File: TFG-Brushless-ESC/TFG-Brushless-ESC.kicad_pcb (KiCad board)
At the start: 2 copper layers, 66 parts, among them J2 USB C Receptacle, J3 SWD, Q1 IRF1310, Q2 IRF1310, Q3 IRF1310, Q4 IRF1310, Q5 IRF1310, Q6 IRF1310, SW1 BOOT0, SW2 NRST, SW3 USER, U1 LM317, U2 STM32F411CEUx, U3 IR2101, U4 IR2101, U5 IR2101, Y1 25MHz, Y2 32.768kHz

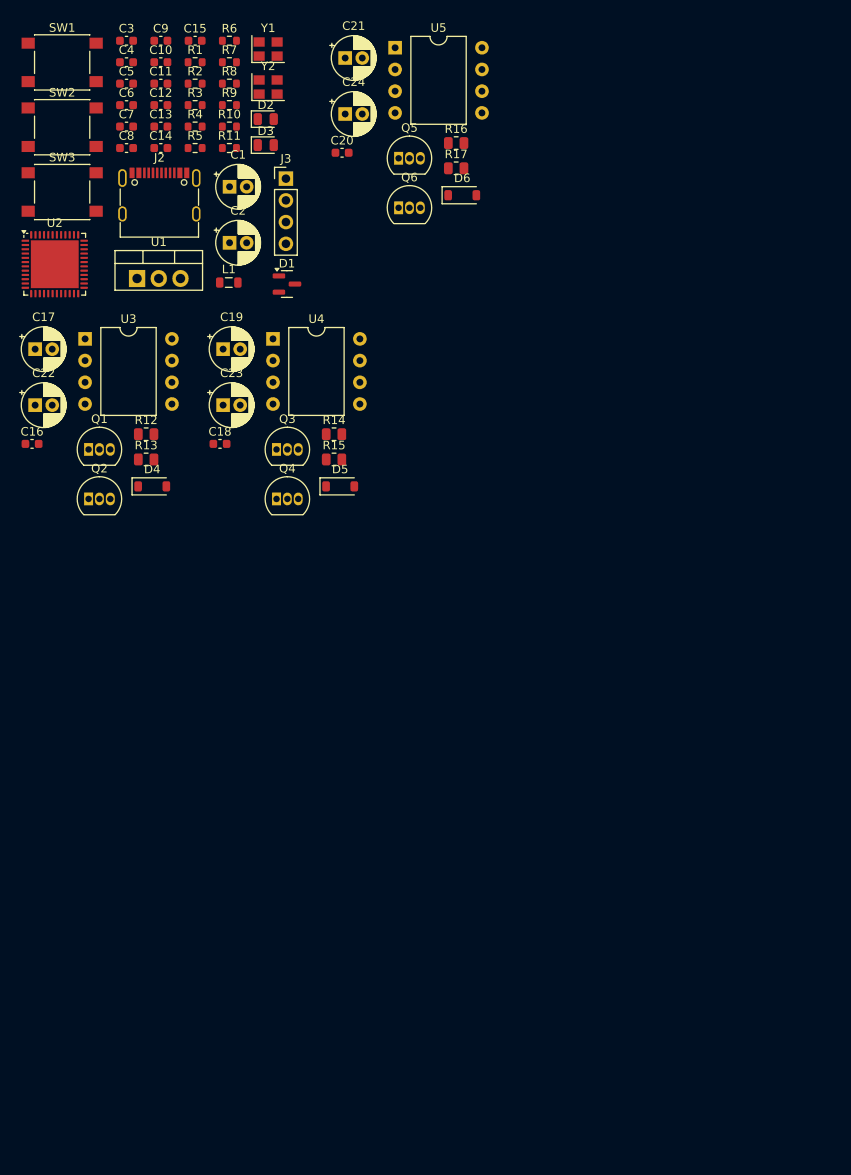
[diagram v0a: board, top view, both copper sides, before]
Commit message: STM and Eeschema changes
STM tests and fixed MOSFET error in Half Bridge
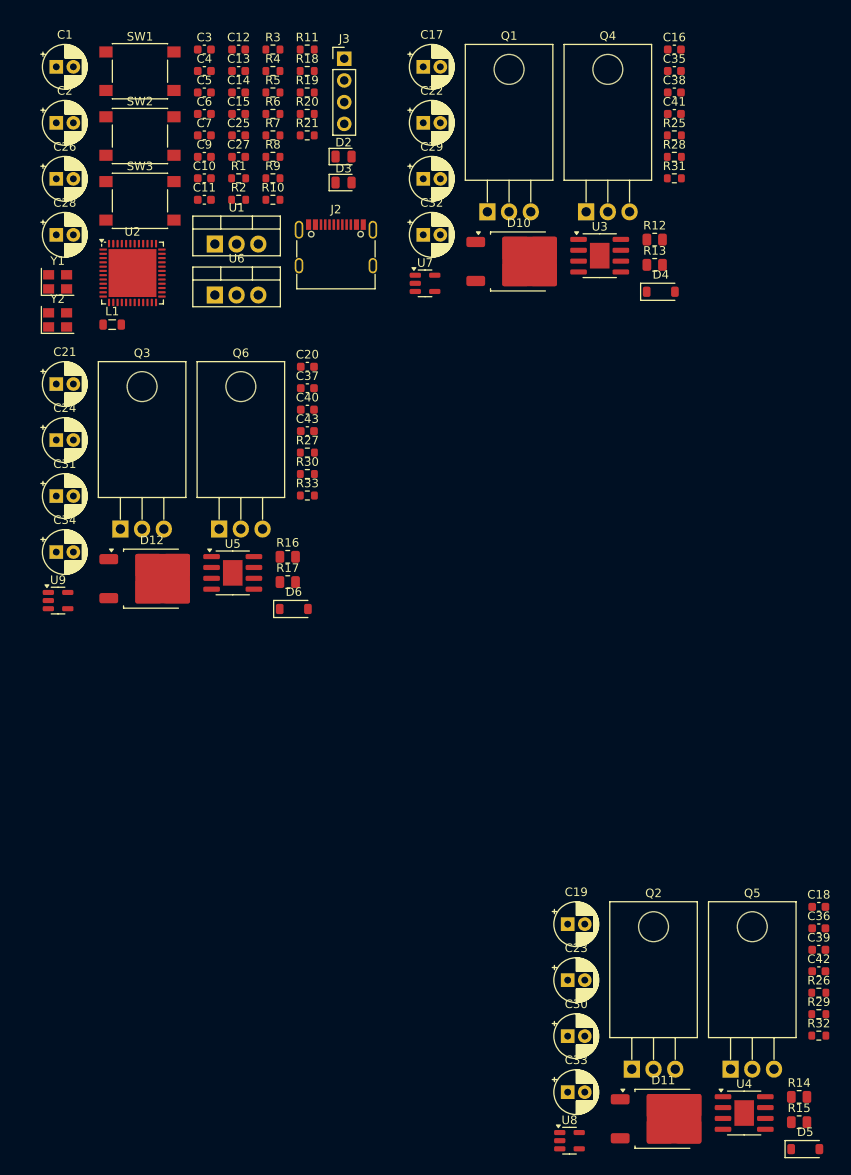
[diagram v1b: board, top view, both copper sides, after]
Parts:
- removed C8: 100n, Capacitor_SMD:C_0603_1608Metric
- removed D1: BAT54C, Package_TO_SOT_SMD:SOT-23
- added C25: 100n, Capacitor_SMD:C_0603_1608Metric, F.Cu at (45.5, 30.4)
- added C26: 220u, Capacitor_THT:CP_Radial_D5.0mm_P2.00mm, F.Cu at (24.1, 35.5)
- added C27: 100n, Capacitor_SMD:C_0603_1608Metric, F.Cu at (45.5, 33.0)
- added C28: 10u, Capacitor_THT:CP_Radial_D5.0mm_P2.00mm, F.Cu at (24.1, 42.1)
- added C29: 10u, Capacitor_THT:CP_Radial_D5.0mm_P2.00mm, F.Cu at (67.1, 35.5)
- added C30: 10u, Capacitor_THT:CP_Radial_D5.0mm_P2.00mm, F.Cu at (84.0, 135.8)
- added C31: 10u, Capacitor_THT:CP_Radial_D5.0mm_P2.00mm, F.Cu at (24.1, 72.6)
- added C32: 47u, Capacitor_THT:CP_Radial_D5.0mm_P2.00mm, F.Cu at (67.1, 42.1)
- added C33: 47u, Capacitor_THT:CP_Radial_D5.0mm_P2.00mm, F.Cu at (84.0, 142.3)
- added C34: 47u, Capacitor_THT:CP_Radial_D5.0mm_P2.00mm, F.Cu at (24.1, 79.2)
- added C35: 100n, Capacitor_SMD:C_0603_1608Metric, F.Cu at (96.4, 22.9)
- added C36: 100n, Capacitor_SMD:C_0603_1608Metric, F.Cu at (113.3, 123.2)
- added C37: 100n, Capacitor_SMD:C_0603_1608Metric, F.Cu at (53.5, 60.0)
- added C38: 10p, Capacitor_SMD:C_0603_1608Metric, F.Cu at (96.4, 25.4)
- added C39: 10p, Capacitor_SMD:C_0603_1608Metric, F.Cu at (113.3, 125.7)
- added C40: 10p, Capacitor_SMD:C_0603_1608Metric, F.Cu at (53.5, 62.5)
- added C41: 100n, Capacitor_SMD:C_0603_1608Metric, F.Cu at (96.4, 27.9)
- added C42: 100n, Capacitor_SMD:C_0603_1608Metric, F.Cu at (113.3, 128.2)
- added C43: 100n, Capacitor_SMD:C_0603_1608Metric, F.Cu at (53.5, 65.0)
- added D10: FERD30H100SB, Package_TO_SOT_SMD:TO-252-2, F.Cu at (78.2, 45.2)
- added D11: FERD30H100SB, Package_TO_SOT_SMD:TO-252-2, F.Cu at (95.1, 145.5)
- added D12: FERD30H100SB, Package_TO_SOT_SMD:TO-252-2, F.Cu at (35.3, 82.3)
- added R18: 390R 1%, Resistor_SMD:R_0603_1608Metric, F.Cu at (53.5, 22.9)
- added R19: 390R 1%, Resistor_SMD:R_0603_1608Metric, F.Cu at (53.5, 25.4)
- added R20: 390R 1%, Resistor_SMD:R_0603_1608Metric, F.Cu at (53.5, 27.9)
- added R21: 10k 1%, Resistor_SMD:R_0603_1608Metric, F.Cu at (53.5, 30.4)
- added R25: 10k, Resistor_SMD:R_0603_1608Metric, F.Cu at (96.4, 30.4)
- added R26: 10k, Resistor_SMD:R_0603_1608Metric, F.Cu at (113.3, 130.7)
- added R27: 10k, Resistor_SMD:R_0603_1608Metric, F.Cu at (53.5, 67.5)
- added R28: 10k, Resistor_SMD:R_0603_1608Metric, F.Cu at (96.4, 33.0)
- added R29: 10k, Resistor_SMD:R_0603_1608Metric, F.Cu at (113.3, 133.2)
- added R30: 10k, Resistor_SMD:R_0603_1608Metric, F.Cu at (53.5, 70.1)
- added R31: 1k, Resistor_SMD:R_0603_1608Metric, F.Cu at (96.4, 35.5)
- added R32: 1k, Resistor_SMD:R_0603_1608Metric, F.Cu at (113.3, 135.7)
- added R33: 1k, Resistor_SMD:R_0603_1608Metric, F.Cu at (53.5, 72.6)
- added U6: LM317, Package_TO_SOT_THT:TO-220-3_Vertical, F.Cu at (42.7, 49.1)
- added U7: INA180A3, Package_TO_SOT_SMD:SOT-23-5, F.Cu at (67.3, 47.8)
- added U8: INA180A3, Package_TO_SOT_SMD:SOT-23-5, F.Cu at (84.2, 148.0)
- added U9: INA180A3, Package_TO_SOT_SMD:SOT-23-5, F.Cu at (24.4, 84.9)
- C17, C19, C21: value 2.2u -> 47u
- Q1, Q2, Q3, Q4, Q5, Q6: value IRF1310 -> TK58E06N1; footprint Package_TO_SOT_THT:TO-92_Inline -> Package_TO_SOT_THT:TO-220-3_Horizontal_TabDown
- U3, U4, U5: footprint Package_DIP:DIP-8_W10.16mm -> Package_SO:SOIC-8-1EP_3.9x4.9mm_P1.27mm_EP2.29x3mm
- moved Q5 113.4 mm to (103.0, 139.7)
- moved U4 106.0 mm to (104.6, 144.8)
- moved R15 94.7 mm to (111.0, 145.9)
- moved D5 94.7 mm to (111.7, 149.0)
- moved R14 94.7 mm to (111.0, 142.9)
- moved Q2 92.1 mm to (91.5, 139.7)
- moved C18 88.5 mm to (113.3, 120.7)
- moved C16 88.1 mm to (96.4, 20.4)
- moved C19 78.4 mm to (84.0, 122.7)
- moved C23 78.4 mm to (84.0, 129.2)
- moved U5 64.3 mm to (44.8, 81.6)
- moved R12 63.7 mm to (94.1, 42.6)
- moved R13 63.7 mm to (94.1, 45.6)
- moved D4 63.7 mm to (94.8, 48.7)
- moved U3 61.0 mm to (87.7, 44.5)
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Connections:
- C16 pad 1: +5V -> +12V
- C18 pad 1: +5V -> +12V
- C20 pad 1: +5V -> +12V
- C22 pad 1: +5V -> +12V
- C23 pad 1: +5V -> +12V
- C24 pad 1: +5V -> +12V
- D4 pad 2: +5V -> +12V
- D5 pad 2: +5V -> +12V
- D6 pad 2: +5V -> +12V
- J2 pad S1: GND -> unconnected-(J2-SHIELD-PadS1)
- Q1 pad 3: +48V -> +24V
- Q2 pad 1: GND -> /V
- Q2 pad 3: /U -> +24V
- Q3 pad 1: /V -> /W
- Q3 pad 3: +48V -> +24V
- Q4 pad 1: GND -> Net-(Q4-S)
- Q4 pad 3: /V -> /U
- Q5 pad 1: /W -> Net-(Q5-S)
- Q5 pad 3: +48V -> /V
- Q6 pad 1: GND -> Net-(Q6-S)
- R13 pad 2: Net-(Q2-G) -> Net-(Q4-G)
- R14 pad 2: Net-(Q3-G) -> Net-(Q2-G)
- R15 pad 2: Net-(Q4-G) -> Net-(Q5-G)
- R16 pad 2: Net-(Q5-G) -> Net-(Q3-G)
- U3 pad 1: +5V -> +12V
- U3 pad 2: /PA5 -> /PA6
- U3 pad 3: /PA6 -> /PA10
- U4 pad 1: +5V -> +12V
- U4 pad 3: /PB0 -> /PA9
- U5 pad 1: +5V -> +12V
- U5 pad 2: /PB1 -> /PB0
- U5 pad 3: /PB10 -> /PA8

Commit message: Half bridges done
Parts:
- removed C43: 100n, Capacitor_SMD:C_0603_1608Metric
- removed D12: FERD30H100SB, Package_TO_SOT_SMD:TO-252-2
- removed SW3: USER, Button_Switch_SMD:SW_Push_1P1T_NO_6x6mm_H9.5mm
- added C8: 100n, Capacitor_SMD:C_0603_1608Metric, F.Cu at (24.1, 24.5)
- added D1: GREEN, LED_SMD:LED_0805_2012Metric, F.Cu at (29.4, 51.6)
- added D7: FERD30H100SB, Package_TO_SOT_SMD:TO-252-2, F.Cu at (186.5, 135.8)
- added D8: PESD-0603-240, Diode_SMD:D_0603_1608Metric, F.Cu at (171.3, 138.7)
- added D9: 1N4148, Diode_SMD:D_SOD-123, F.Cu at (215.1, 133.8)
- added J1: 24V IN, TFG-Brushless-ESC:Large_Conn_01x02, F.Cu at (136.1, 121.0)
- added J4: W, TFG-Brushless-ESC:Large_Conn_01x01, F.Cu at (194.6, 119.1)
- added J5: USB C Receptacle, Connector_USB:USB_C_Receptacle_G-Switch_GT-USB-7010ASV, F.Cu at (50.6, 53.2)
- added J6: HALL SENSORS, Connector_PinHeader_2.54mm:PinHeader_1x05_P2.54mm_Vertical, F.Cu at (58.1, 23.0)
- added J7: SWD, Connector_PinHeader_2.54mm:PinHeader_1x04_P2.54mm_Vertical, F.Cu at (40.5, 49.2)
- added R22: 100R, Resistor_SMD:R_0805_2012Metric, F.Cu at (179.3, 136.1)
- added R23: 10k, Resistor_SMD:R_0603_1608Metric, F.Cu at (159.6, 135.3)
- added R24: 100R, Resistor_SMD:R_0805_2012Metric, F.Cu at (167.5, 135.4)
- C1: value 220u -> 100n; footprint Capacitor_THT:CP_Radial_D5.0mm_P2.00mm -> Capacitor_SMD:C_0603_1608Metric
- C11, C12: value 20p -> 100n
- C13: value 12p5 -> 100n
- C14: value 12p5 -> 20p
- C15: value 2u2 -> 20p
- C16: value 100n -> 12p5
- C17: value 47u -> 12p5; footprint Capacitor_THT:CP_Radial_D5.0mm_P2.00mm -> Capacitor_SMD:C_0603_1608Metric
- C18: value 100n -> 2u2
- C19: value 47u -> 2.2u
- C2: value 10u -> 220u
- C22: value 2.2u -> 47u
- C23: value 2.2u -> 100n; footprint Capacitor_THT:CP_Radial_D5.0mm_P2.00mm -> Capacitor_SMD:C_0603_1608Metric
- C24: value 2.2u -> 10u
- C26: value 220u -> 10p; footprint Capacitor_THT:CP_Radial_D5.0mm_P2.00mm -> Capacitor_SMD:C_0603_1608Metric
- C27, C35: value 100n -> 2.2u; footprint Capacitor_SMD:C_0603_1608Metric -> Capacitor_THT:CP_Radial_D5.0mm_P2.00mm
- C28, C31: value 10u -> 100n; footprint Capacitor_THT:CP_Radial_D5.0mm_P2.00mm -> Capacitor_SMD:C_0603_1608Metric
- C29, C30: value 10u -> 47u
- C3, C6: value 100n -> 10u; footprint Capacitor_SMD:C_0603_1608Metric -> Capacitor_THT:CP_Radial_D5.0mm_P2.00mm
- C32: value 47u -> 10u
- C33: value 47u -> 100n; footprint Capacitor_THT:CP_Radial_D5.0mm_P2.00mm -> Capacitor_SMD:C_0603_1608Metric
- C34: value 47u -> 10p; footprint Capacitor_THT:CP_Radial_D5.0mm_P2.00mm -> Capacitor_SMD:C_0603_1608Metric
- C37: value 100n -> 47u; footprint Capacitor_SMD:C_0603_1608Metric -> Capacitor_THT:CP_Radial_D5.0mm_P2.00mm
- C38: value 10p -> 47u; footprint Capacitor_SMD:C_0603_1608Metric -> Capacitor_THT:CP_Radial_D5.0mm_P2.00mm
- C39: value 10p -> 100n
- C40: value 10p -> 10u; footprint Capacitor_SMD:C_0603_1608Metric -> Capacitor_THT:CP_Radial_D5.0mm_P2.00mm
- C42: value 100n -> 10p
- C5: value 100n -> 220u; footprint Capacitor_SMD:C_0603_1608Metric -> Capacitor_THT:CP_Radial_D5.0mm_P2.00mm
- D11: value FERD30H100SB -> PESD-0603-240; footprint Package_TO_SOT_SMD:TO-252-2 -> Diode_SMD:D_0603_1608Metric
- D3: value GREEN -> 1N4148; footprint LED_SMD:LED_0805_2012Metric -> Diode_SMD:D_SOD-123
- D4: value 1N4148 -> FERD30H100SB; footprint Diode_SMD:D_SOD-123 -> Package_TO_SOT_SMD:TO-252-2
- D5: value 1N4148 -> PESD-0603-240; footprint Diode_SMD:D_SOD-123 -> Diode_SMD:D_0603_1608Metric
- J2: value USB C Receptacle -> U; footprint Connector_USB:USB_C_Receptacle_G-Switch_GT-USB-7010ASV -> TFG-Brushless-ESC:Large_Conn_01x01
- J3: value SWD -> V; footprint Connector_PinHeader_2.54mm:PinHeader_1x04_P2.54mm_Vertical -> TFG-Brushless-ESC:Large_Conn_01x01
- Q1, Q2, Q3, Q4, Q5, Q6: footprint Package_TO_SOT_THT:TO-220-3_Horizontal_TabDown -> Package_TO_SOT_THT:TO-220-3_Vertical
- R10: value 1k -> 5k1
- R11: value 1k -> 22R
- R12: value 100R -> 22R; footprint Resistor_SMD:R_0805_2012Metric -> Resistor_SMD:R_0603_1608Metric
- R13, R17: value 100R -> 10k; footprint Resistor_SMD:R_0805_2012Metric -> Resistor_SMD:R_0603_1608Metric
- R14, R15: value 100R -> 1k; footprint Resistor_SMD:R_0805_2012Metric -> Resistor_SMD:R_0603_1608Metric
- R18: value 390R 1% -> 100R; footprint Resistor_SMD:R_0603_1608Metric -> Resistor_SMD:R_0805_2012Metric
- R19: value 390R 1% -> 1k
- R2, R4: value 10k -> 390R 1%
- R20: value 390R 1% -> 2mR; footprint Resistor_SMD:R_0603_1608Metric -> Resistor_SMD:R_2512_6332Metric
- R21: value 10k 1% -> 10k
- R25: value 10k -> 1k
- R26: value 10k -> 2mR; footprint Resistor_SMD:R_0603_1608Metric -> Resistor_SMD:R_2512_6332Metric
- R28, R30: value 10k -> 100R; footprint Resistor_SMD:R_0603_1608Metric -> Resistor_SMD:R_0805_2012Metric
- R32: value 1k -> 2mR; footprint Resistor_SMD:R_0603_1608Metric -> Resistor_SMD:R_2512_6332Metric
- R33: value 1k -> 10k
- R5: value 5k1 -> 10k
- R6: value 5k1 -> 390R 1%
- R7: value 22R -> 10k 1%
- R8: value 22R -> 10k
- R9: value 10k -> 5k1
- U2: value STM32F411CEUx -> LM317; footprint Package_DFN_QFN:QFN-48-1EP_7x7mm_P0.5mm_EP5.6x5.6mm -> Package_TO_SOT_THT:TO-220-3_Vertical
- U3: value IR2101 -> STM32F411CEUx; footprint Package_SO:SOIC-8-1EP_3.9x4.9mm_P1.27mm_EP2.29x3mm -> Package_DFN_QFN:QFN-48-1EP_7x7mm_P0.5mm_EP5.6x5.6mm
- U5: value IR2101 -> INA180A3; footprint Package_SO:SOIC-8-1EP_3.9x4.9mm_P1.27mm_EP2.29x3mm -> Package_TO_SOT_SMD:SOT-23-5
- U6: value LM317 -> IR2101; footprint Package_TO_SOT_THT:TO-220-3_Vertical -> Package_SO:SOIC-8-1EP_3.9x4.9mm_P1.27mm_EP2.29x3mm
- U8: value INA180A3 -> IR2101; footprint Package_TO_SOT_SMD:SOT-23-5 -> Package_SO:SOIC-8-1EP_3.9x4.9mm_P1.27mm_EP2.29x3mm
- moved U9 186.2 mm to (204.5, 131.9)
- moved C40 183.5 mm to (224.6, 129.0), turned to 90 degrees
- moved C37 176.8 mm to (216.0, 129.8), turned to 180 degrees
- moved Q6 173.9 mm to (205.5, 138.8), turned to 180 degrees
- moved D10 172.1 mm to (224.6, 135.8), turned to 90 degrees
- moved C28 169.5 mm to (171.3, 126.2), turned to 180 degrees
- moved R30 165.4 mm to (205.5, 135.4), turned to -90 degrees
- moved Q3 161.1 mm to (180.2, 138.7), turned to 180 degrees
- moved C27 160.5 mm to (177.0, 124.9), turned to 90 degrees
- moved R33 160.0 mm to (203.4, 128.5), turned to 90 degrees
- moved R28 158.9 mm to (217.3, 136.2)
- moved C35 156.4 mm to (215.1, 124.9), turned to 90 degrees
- moved C31 154.0 mm to (167.6, 128.5), turned to 90 degrees
- moved U6 153.0 mm to (171.3, 131.9), turned to -90 degrees
- moved C38 150.4 mm to (195.3, 138.8), turned to 180 degrees
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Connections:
- C10 pad 1: GND -> +3V3
- C10 pad 2: /NRST -> GND
- C11 pad 1: /HSE_1 -> +3V3
- C12 pad 1: /HSE_2 -> /VDDA
- C13 pad 1: /LSE_1 -> GND
- C13 pad 2: GND -> /NRST
- C14 pad 1: /LSE_2 -> /HSE_1
- C15 pad 1: /VCAP1 -> /HSE_2
- C16 pad 1: +12V -> /LSE_1
- C17 pad 1: Net-(D4-K) -> /LSE_2
- C17 pad 2: /U -> GND
- C18 pad 1: +12V -> /VCAP1
- C19 pad 1: Net-(D5-K) -> +12V
- C19 pad 2: /V -> GND
- C2 pad 1: +3V3 -> +5V
- C21 pad 1: Net-(D6-K) -> Net-(D3-K)
- C21 pad 2: /W -> /U
- C22 pad 1: +12V -> /U
- C23 pad 1: +12V -> +3V3
- C24 pad 1: +12V -> +24V
- C25 pad 1: +48V -> /PA3
- C26 pad 1: +48V -> GND
- C26 pad 2: GND -> /PA0
- C27 pad 1: +5V -> +12V
- C29 pad 1: +24V -> Net-(D6-K)
- C29 pad 2: GND -> /V
- C3 pad 1: GND -> +3V3
- C3 pad 2: /BOOT0 -> GND
- C30 pad 1: +24V -> /V
- C31 pad 1: +24V -> +3V3
- C33 pad 1: +24V -> /PA4
- C34 pad 1: +24V -> GND
- C34 pad 2: GND -> /PA1
- C35 pad 1: +3V3 -> +12V
- C36 pad 1: +3V3 -> +12V
- C37 pad 1: +3V3 -> Net-(D9-K)
- C37 pad 2: GND -> /W
- C38 pad 1: GND -> /W
- C38 pad 2: /PA0 -> GND
- C39 pad 1: GND -> +3V3
- C39 pad 2: /PA1 -> GND
- C4 pad 1: +3V3 -> +48V
- C40 pad 1: GND -> +24V
- C40 pad 2: /PA2 -> GND
- C41 pad 1: /PA3 -> /PA5
- C42 pad 1: /PA4 -> GND
- C42 pad 2: GND -> /PA2
- C5 pad 1: +3V3 -> +48V
- C6 pad 1: +3V3 -> +12V
- C7 pad 1: +3V3 -> GND
- C7 pad 2: GND -> /BOOT0
- C9 pad 1: /VDDA -> +3V3
- D10 pad 1: /U -> /W
- D10 pad 3: /U -> /W
- D11 pad 1: /V -> GND
- D11 pad 2: +24V -> /W
- D2 pad 1: GND -> /PC13
- D3 pad 1: /PC13 -> Net-(D3-K)
- D3 pad 2: Net-(D3-A) -> +12V
- D4 pad 1: Net-(D4-K) -> /U
- D4 pad 2: +12V -> +24V
- D5 pad 1: Net-(D5-K) -> GND
- D5 pad 2: +12V -> /U
- J3 pad 1: +3V3 -> /V
- Q1 pad 1: /U -> Net-(Q1-G)
- Q1 pad 2: Net-(Q1-G) -> +24V
- Q1 pad 3: +24V -> /U
- Q2 pad 1: /V -> Net-(Q2-G)
- Q2 pad 2: Net-(Q2-G) -> /U
- Q2 pad 3: +24V -> /Half-Bridge-U/Shunt
- Q3 pad 1: /W -> Net-(Q3-G)
- Q3 pad 2: Net-(Q3-G) -> +24V
- Q3 pad 3: +24V -> /V
- Q4 pad 1: Net-(Q4-S) -> Net-(Q4-G)
- Q4 pad 2: Net-(Q4-G) -> /V
- Q4 pad 3: /U -> /Half-Bridge-V/Shunt
- Q5 pad 1: Net-(Q5-S) -> Net-(Q5-G)
- Q5 pad 2: Net-(Q5-G) -> +24V
- Q5 pad 3: /V -> /W
- Q6 pad 1: Net-(Q6-S) -> Net-(Q6-G)
- Q6 pad 2: Net-(Q6-G) -> /W
- Q6 pad 3: /W -> /Half-Bridge-W/Shunt
- R10 pad 1: +3V3 -> GND
- R10 pad 2: Net-(D2-A) -> /USB_CC2
- R11 pad 1: +3V3 -> /USB_N
- R11 pad 2: Net-(D3-A) -> Net-(J5-D--PadA7)
- R12 pad 1: Net-(U3-HO) -> /USB_P
- R12 pad 2: Net-(Q1-G) -> Net-(J5-D+-PadA6)
- R13 pad 1: Net-(U3-LO) -> /BOOT1
- R13 pad 2: Net-(Q4-G) -> GND
- R14 pad 1: Net-(U4-HO) -> +3V3
- R14 pad 2: Net-(Q2-G) -> Net-(D1-A)
- R15 pad 1: Net-(U4-LO) -> +3V3
- R15 pad 2: Net-(Q5-G) -> Net-(D2-A)
- R16 pad 1: Net-(U5-HO) -> Net-(U4-HO)
- R16 pad 2: Net-(Q3-G) -> Net-(Q1-G)
- R17 pad 1: Net-(U5-LO) -> /PA3
- R17 pad 2: Net-(Q6-G) -> /U
- R18 pad 1: +12V -> Net-(U4-LO)
- R18 pad 2: /V_DIV -> Net-(Q2-G)
- R19 pad 1: +12V -> GND
- R19 pad 2: /V_DIV -> /PA3
- R2 pad 1: GND -> +12V
- R2 pad 2: /BOOT0 -> /V_DIV
- R20 pad 1: +12V -> /Half-Bridge-U/Shunt
- R20 pad 2: /V_DIV -> GND
- R21 pad 1: GND -> Net-(R21-Pad1)
- R21 pad 2: /V_DIV -> /PA0
- R25 pad 1: Net-(R25-Pad1) -> GND
- R25 pad 2: /PA0 -> /PA4
- R26 pad 1: Net-(R26-Pad1) -> /Half-Bridge-V/Shunt
- R26 pad 2: /PA1 -> GND
- R27 pad 2: /PA2 -> /PA1
- R28 pad 1: /PA3 -> Net-(U8-HO)
- R28 pad 2: /U -> Net-(Q5-G)
- R29 pad 1: /PA4 -> /PA5
- R29 pad 2: /V -> /W
- R3 pad 1: /V_DIV -> +12V
- R3 pad 2: GND -> /V_DIV
- R30 pad 1: /PA5 -> Net-(U8-LO)
- R30 pad 2: /W -> Net-(Q6-G)
- R31 pad 2: /PA3 -> /PA5
- R32 pad 1: GND -> /Half-Bridge-W/Shunt
- R32 pad 2: /PA4 -> GND
- R33 pad 1: GND -> Net-(R33-Pad1)
- R33 pad 2: /PA5 -> /PA2
- R4 pad 1: +3V3 -> +12V
- R4 pad 2: /NRST -> /V_DIV
- R5 pad 2: /USB_CC1 -> /BOOT0
- R6 pad 1: GND -> /V_DIV
- R6 pad 2: /USB_CC2 -> GND
- R7 pad 1: /USB_N -> GND
- R7 pad 2: Net-(J2-D--PadA7) -> /V_DIV
- R8 pad 1: /USB_P -> +3V3
- R8 pad 2: Net-(J2-D+-PadA6) -> /NRST
- R9 pad 1: /BOOT1 -> GND
- R9 pad 2: GND -> /USB_CC1
- U2 pad 1: /VBAT -> /V_DIV
- U2 pad 2: /PC13 -> +12V
- U2 pad 3: /LSE_1 -> +48V
- U3 pad 1: +12V -> /VBAT
- U3 pad 2: /PA6 -> /PC13
- U3 pad 3: /PA10 -> /LSE_1
- U3 pad 4: GND -> /LSE_2
- U3 pad 5: Net-(U3-LO) -> /HSE_1
- U3 pad 6: /U -> /HSE_2
- U3 pad 7: Net-(U3-HO) -> /BOOT0
- U3 pad 8: Net-(D4-K) -> GND
- U3 pad 9: (no net) -> /VDDA
- U4 pad 2: /PA7 -> /PA6
- U4 pad 3: /PA9 -> /PA10
- U4 pad 6: /V -> /U
- U4 pad 8: Net-(D5-K) -> Net-(D3-K)
- U5 pad 1: +12V -> Net-(R21-Pad1)
- U5 pad 2: /PB0 -> GND
- U5 pad 3: /PA8 -> /Half-Bridge-U/Shunt
- U5 pad 5: Net-(U5-LO) -> +3V3
- U6 pad 1: /V_DIV -> +12V
- U6 pad 2: +12V -> /PA7
- U6 pad 3: +48V -> /PA9
- U7 pad 1: Net-(R25-Pad1) -> Net-(R27-Pad1)
- U7 pad 3: Net-(Q4-S) -> /Half-Bridge-V/Shunt
- U8 pad 1: Net-(R26-Pad1) -> +12V
- U8 pad 2: GND -> /PB0
- U8 pad 3: Net-(Q5-S) -> /PA8
- U8 pad 5: +3V3 -> Net-(U8-LO)
- U9 pad 1: Net-(R27-Pad1) -> Net-(R33-Pad1)
- U9 pad 3: Net-(Q6-S) -> /Half-Bridge-W/Shunt
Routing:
- net GND: track 0.00 -> 151.1 mm, vias 0 -> 30
- net +12V: track 0.00 -> 51.7 mm
- net /U: track 0.00 -> 41.9 mm, vias 0 -> 4
- net /W: track 0.00 -> 41.9 mm, vias 0 -> 4
- net /V: track 0.00 -> 41.9 mm, vias 0 -> 4
- net /PA3: track 0.00 -> 13.0 mm, vias 0 -> 1
- net /PA4: track 0.00 -> 12.9 mm, vias 0 -> 1
- net /PA5: track 0.00 -> 12.9 mm, vias 0 -> 1
- net Net-(D6-K): track 0.00 -> 12.7 mm
- net Net-(D3-K): track 0.00 -> 12.7 mm
- net Net-(D9-K): track 0.00 -> 12.7 mm
- net +3V3: track 0.00 -> 8.97 mm, vias 0 -> 3
- net Net-(U6-HO): track 0.00 -> 7.78 mm
- net Net-(U8-HO): track 0.00 -> 7.78 mm
- net Net-(U4-HO): track 0.00 -> 7.78 mm
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- added copper zone on F.Cu, net +24V
- added copper zone on In2.Cu, net +24V
- added copper zone on F.Cu, net /Half-Bridge-U/Shunt
- added copper zone on F.Cu, net /Half-Bridge-V/Shunt
- added copper zone on F.Cu, net /Half-Bridge-W/Shunt
- added copper zone on F.Cu, net /U
- added copper zone on In2.Cu, net /U
- added copper zone on F.Cu, net /V
- added copper zone on In2.Cu, net /V
- added copper zone on F.Cu, net /W
- added copper zone on In2.Cu, net /W
- added copper zone on F.Cu, net GND
- added copper zone on In1.Cu, net GND
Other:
- board outline added: 282.6 x 193.9 mm
- copper layers 2 -> 4

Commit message: Switched stackup and routed part of uC
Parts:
- removed C11: 100n, Capacitor_SMD:C_0603_1608Metric
- removed J3: V, TFG-Brushless-ESC:Large_Conn_01x01
- removed J4: W, TFG-Brushless-ESC:Large_Conn_01x01
- added J6: HALL SENSORS, Connector_PinHeader_2.54mm:PinHeader_1x05_P2.54mm_Vertical, F.Cu at (1.82, 1.82)
- J1: footprint TFG-Brushless-ESC:Large_Conn_01x02 -> TerminalBlock_Phoenix:TerminalBlock_Phoenix_MKDS-1,5-2-5.08_1x02_P5.08mm_Horizontal
- J2: value U -> MOTOR; footprint TFG-Brushless-ESC:Large_Conn_01x01 -> TerminalBlock_Phoenix:TerminalBlock_Phoenix_MKDS-1,5-3-5.08_1x03_P5.08mm_Horizontal
- moved C10 177.0 mm to (187.0, 98.6)
- moved C7 175.8 mm to (186.8, 88.4)
- moved C9 175.3 mm to (187.0, 91.8)
- moved R13 173.1 mm to (193.4, 100.1)
- moved C18 172.7 mm to (187.0, 97.1), turned to 180 degrees
- moved R11 169.6 mm to (189.7, 94.9)
- moved R12 168.2 mm to (189.7, 93.4)
- moved C8 167.0 mm to (177.9, 89.5), turned to 90 degrees
- moved R5 166.5 mm to (186.8, 90.0)
- moved C13 164.8 mm to (180.7, 88.4)
- moved R8 164.6 mm to (183.8, 88.4), turned to 180 degrees
- moved U3 162.4 mm to (181.3, 95.2)
- moved C16 161.9 mm to (176.3, 89.5), turned to 90 degrees
- moved C12 161.4 mm to (173.5, 95.8), turned to 180 degrees
- moved C15 160.7 mm to (170.0, 97.4), turned to 180 degrees
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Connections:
- net Net-(J5-D+-PadA6) renamed /USB_R_P
- net Net-(J5-D--PadA7) renamed /USB_R_N
- U3 pad 1: /VBAT -> unconnected-(U3-VBAT-Pad1)
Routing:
- net +3V3: track 8.97 -> 92.8 mm, vias 3 -> 8
- net GND: track 151.1 -> 211.2 mm, vias 30 -> 33
- net /BOOT0: track 0.00 -> 24.4 mm, vias 0 -> 2
- net /NRST: track 0.00 -> 18.3 mm
- net /BOOT1: track 0.00 -> 17.3 mm
- net /PC13: track 0.00 -> 13.8 mm, vias 0 -> 2
- net /HSE_1: track 0.00 -> 11.4 mm
- net /LSE_2: track 0.00 -> 11.3 mm
- net /PB10: track 0.00 -> 11.3 mm
- net /SWSCK: track 0.00 -> 11.2 mm
- net /LSE_1: track 0.00 -> 11.2 mm
- net /HSE_2: track 0.00 -> 10.5 mm
- net /VCAP1: track 0.00 -> 9.48 mm
- net /SWDIO: track 0.00 -> 9.41 mm
- net /PB1: track 0.00 -> 7.40 mm
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- added copper zone on B.Cu, net +24V
- added copper zone on B.Cu, net /U
- added copper zone on B.Cu, net /V
- added copper zone on B.Cu, net /W
- added copper zone on In2.Cu, net GND
- removed copper zone on In2.Cu, net +24V
- removed copper zone on In2.Cu, net /U
- removed copper zone on In2.Cu, net /V
- removed copper zone on In2.Cu, net /W
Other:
- board size 282.6 x 193.9 mm -> 129.3 x 33.1 mm
- board text added: "Inner and outer layers are 1oz"

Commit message: Changes in schematic and pcb
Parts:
- removed D11, D5, D8: PESD-0603-240, Diode_SMD:D_0603_1608Metric
- removed the J6 at (184.1, 102.7)
- removed R13: 10k, Resistor_SMD:R_0603_1608Metric
- added M3: MountingHole_3.2mm_M3_Pad_Via, MountingHole:MountingHole_3.2mm_M3_Pad_Via, F.Cu at (234.0, 138.0)
- added M3: MountingHole_3.2mm_M3_Pad_Via, MountingHole:MountingHole_3.2mm_M3_Pad_Via, F.Cu at (234.0, 98.0)
- added M3: MountingHole_3.2mm_M3_Pad_Via, MountingHole:MountingHole_3.2mm_M3_Pad_Via, F.Cu at (114.0, 98.0)
- added M3: MountingHole_3.2mm_M3_Pad_Via, MountingHole:MountingHole_3.2mm_M3_Pad_Via, F.Cu at (114.0, 138.0)
- added R34: 10k, Resistor_SMD:R_0603_1608Metric, F.Cu at (133.7, 98.0)
- added R35: 10k, Resistor_SMD:R_0603_1608Metric, F.Cu at (132.0, 98.0)
- added R36: 10k, Resistor_SMD:R_0603_1608Metric, F.Cu at (130.2, 98.0)
- J6: footprint Connector_PinHeader_2.54mm:PinHeader_1x05_P2.54mm_Vertical -> Connector_JST:JST_PH_B5B-PH-SM4-TB_1x05-1MP_P2.00mm_Vertical
- moved J6 256.4 mm to (234.2, 110.3), turned to -90 degrees
- moved C4 155.5 mm to (168.5, 98.8)
- moved R2 150.4 mm to (165.1, 101.8), turned to 180 degrees
- moved R3 148.3 mm to (165.1, 100.3)
- moved R7 147.4 mm to (165.1, 103.3), turned to 180 degrees
- moved R4 146.4 mm to (165.1, 98.8), turned to 180 degrees
- moved C5 144.8 mm to (169.5, 102.7), turned to -90 degrees
- moved C1 142.4 mm to (155.3, 98.7)
- moved R6 141.6 mm to (150.2, 100.2)
- moved C2 138.8 mm to (154.8, 102.7), turned to -90 degrees
- moved R1 136.8 mm to (150.2, 98.7), turned to 180 degrees
- moved C6 133.9 mm to (160.7, 102.7), turned to -90 degrees
- moved C3 130.4 mm to (149.1, 102.7), turned to -90 degrees
- moved U2 123.5 mm to (160.7, 96.4)
- moved U1 116.1 mm to (149.4, 96.4)
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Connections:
- net /BOOT1 renamed /PB2
- C4 pad 1: +48V -> +24V
- C5 pad 1: +48V -> +24V
- R1 pad 2: /V_DIV -> /V_DIV_3
- R2 pad 1: +12V -> Net-(U2-VO)
- R2 pad 2: /V_DIV -> Net-(R2-Pad2)
- R3 pad 1: +12V -> Net-(R2-Pad2)
- R3 pad 2: /V_DIV -> Net-(R3-Pad2)
- R4 pad 1: +12V -> Net-(R3-Pad2)
- R4 pad 2: /V_DIV -> +12V
- R6 pad 1: /V_DIV -> /V_DIV_3
- R7 pad 2: /V_DIV -> +12V
- U1 pad 1: /V_DIV -> /V_DIV_3
- U2 pad 1: /V_DIV -> +12V
- U2 pad 2: +12V -> Net-(U2-VO)
- U2 pad 3: +48V -> +24V
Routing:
- net /PB10: track 11.3 -> 134.1 mm
- net /PB1: track 7.40 -> 117.5 mm
- net /PB2: track 17.3 -> 127.2 mm
- net +3V3: track 92.8 -> 116.4 mm, vias 8 -> 12
- net +5V: track 6.95 -> 25.3 mm, vias 0 -> 2
- net +12V: track 51.7 -> 67.8 mm
- net /U: track 44.8 -> 32.9 mm
- net Net-(Q1-G): track 2.46 -> 14.4 mm
- net GND: track 211.2 -> 222.5 mm, vias 33 -> 39
- net /USB_R_N: track 2.99 -> 13.6 mm
- net /USB_R_P: track 2.97 -> 13.6 mm
- net +24V: track 0.00 -> 9.15 mm
- net Net-(U2-VO): track 0.00 -> 8.38 mm
- net /V_DIV_3: track 0.00 -> 3.83 mm
- net Net-(R3-Pad2): track 0.00 -> 1.52 mm
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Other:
- board size 129.3 x 33.1 mm -> 130 x 50 mm
- board text removed: "Inner and outer layers are 1oz"
